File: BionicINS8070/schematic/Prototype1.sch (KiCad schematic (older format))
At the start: 4 parts, among them J1 BionicConnector, U1 INS8070, U2 74HCT126

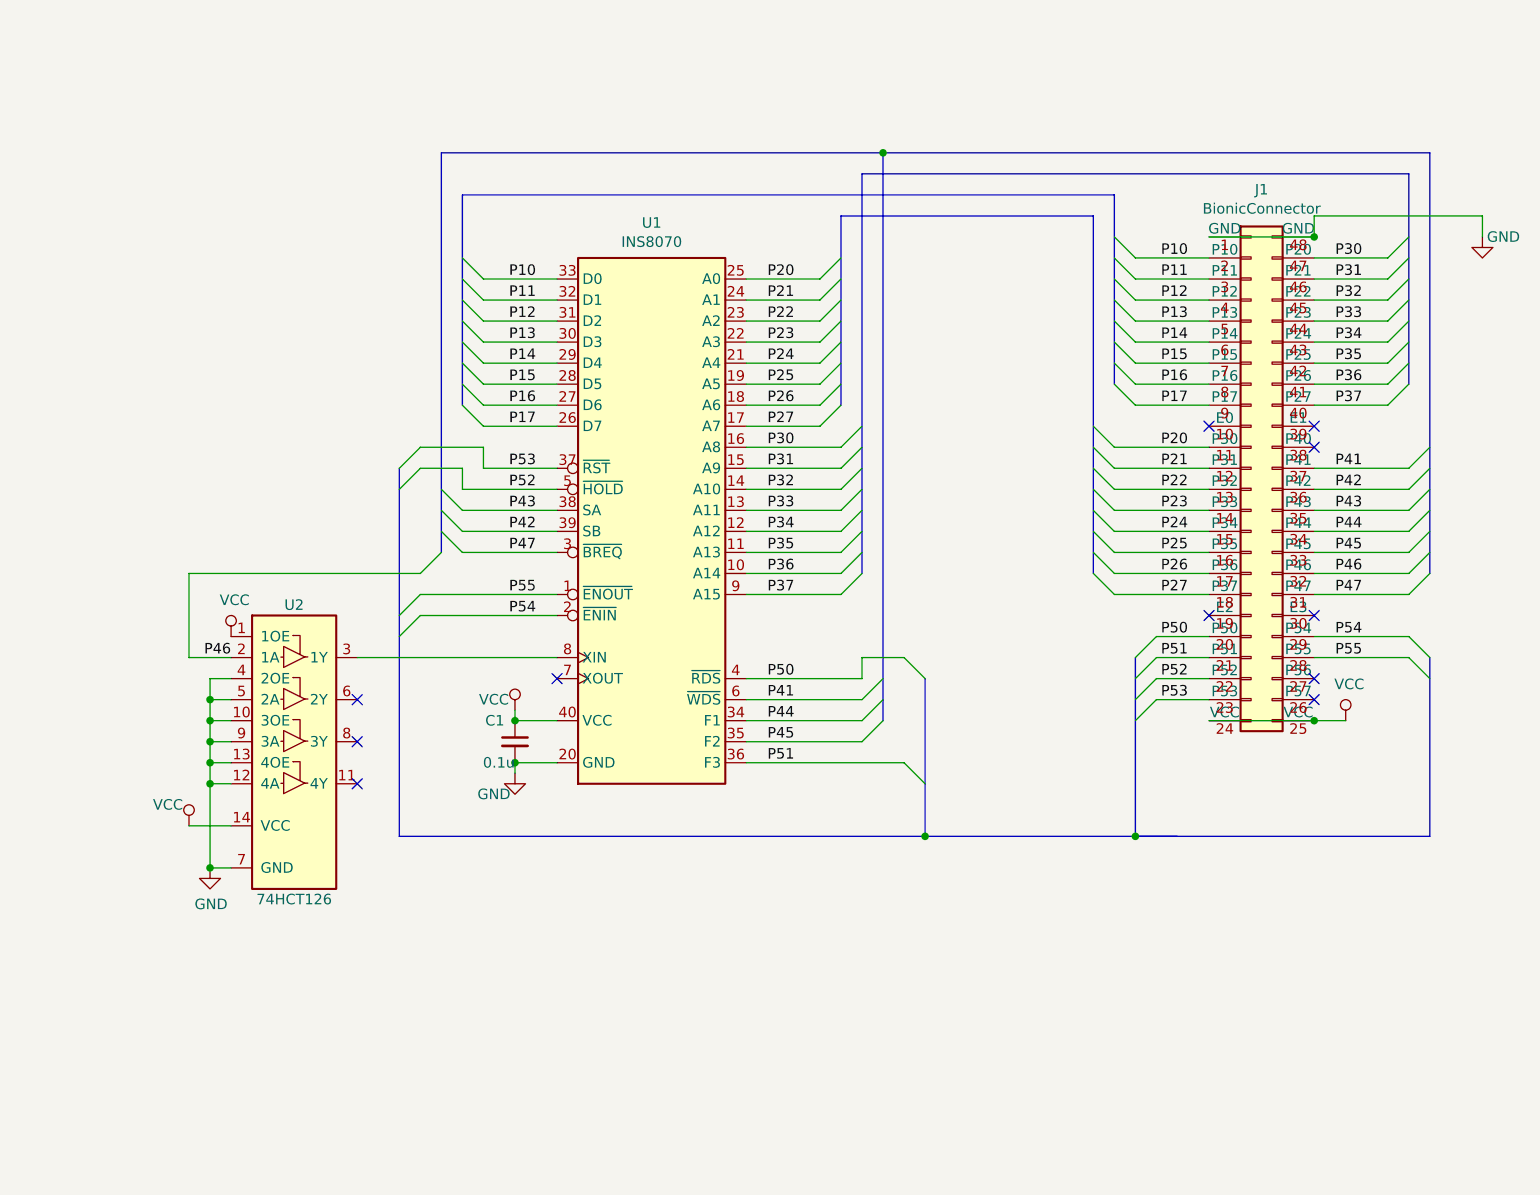
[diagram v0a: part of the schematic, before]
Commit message: Fix Bionic connector pin outs
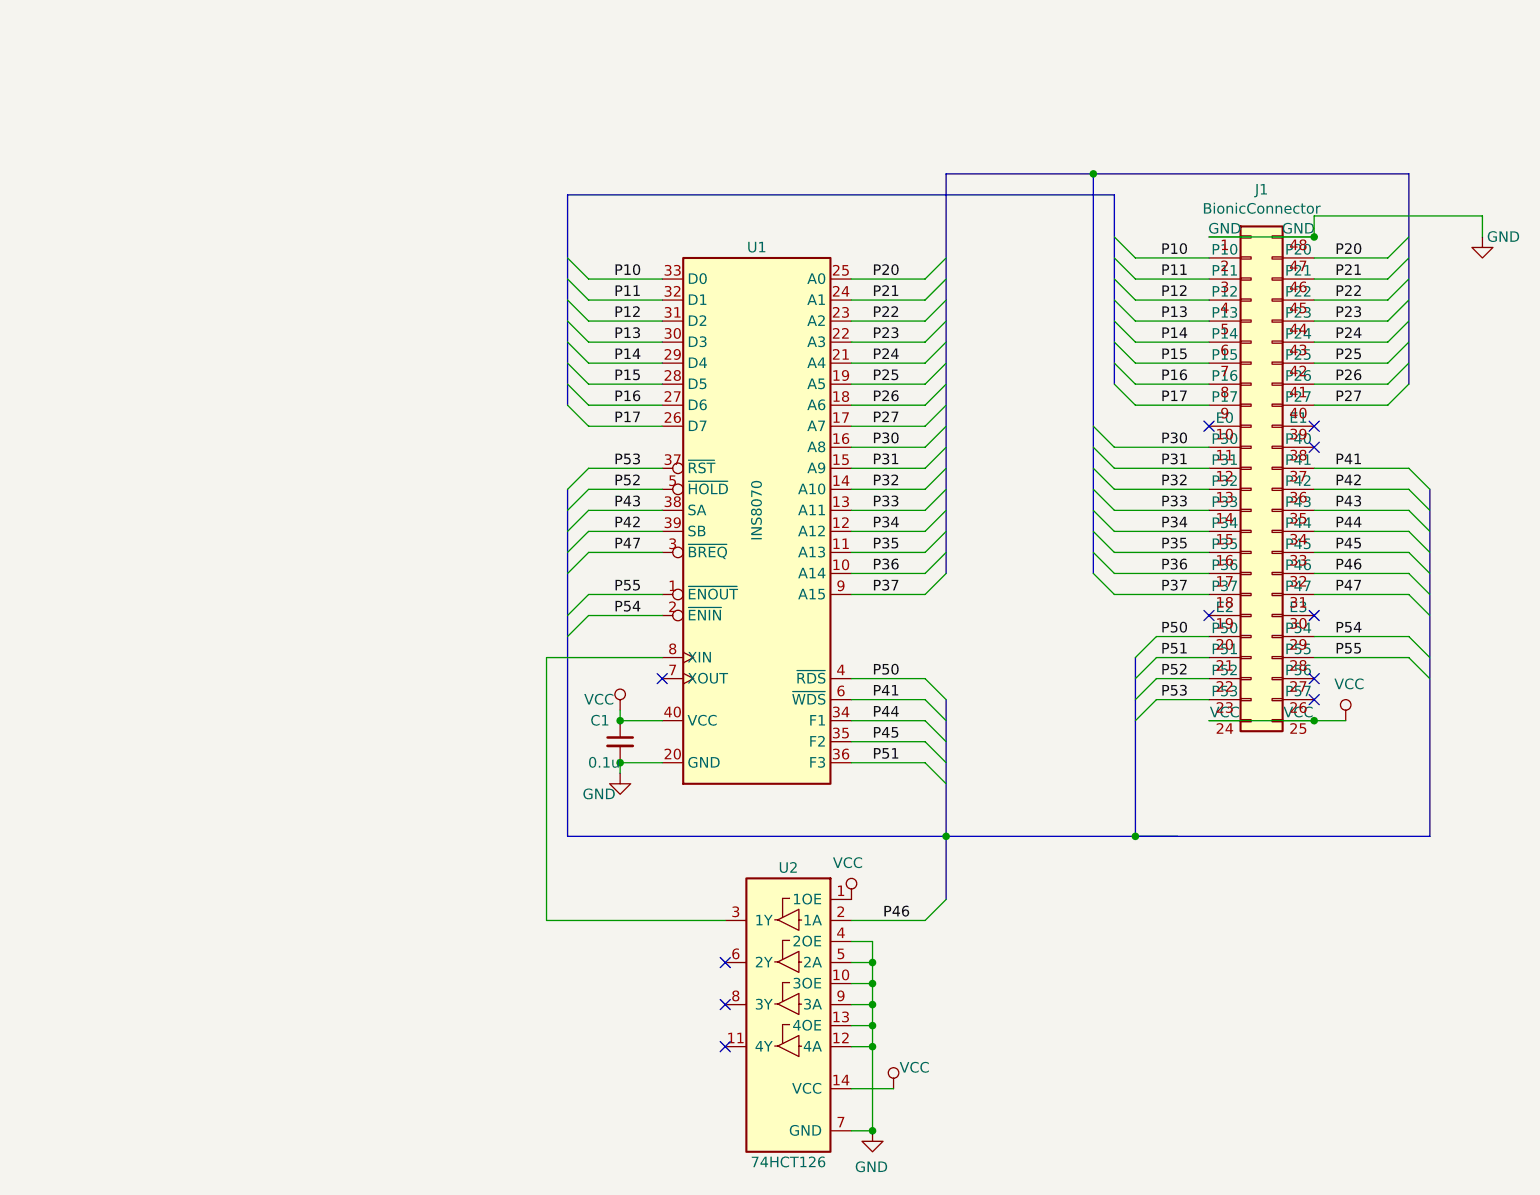
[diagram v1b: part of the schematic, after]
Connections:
- net P20: now also J1.47 (P20); no longer J1.11 (P30)
- net P21: now also J1.46 (P21); no longer J1.12 (P31)
- net P22: now also J1.45 (P22); no longer J1.13 (P32)
- net P23: now also J1.44 (P23); no longer J1.14 (P33)
- net P24: now also J1.43 (P24); no longer J1.15 (P34)
- net P25: now also J1.42 (P25); no longer J1.16 (P35)
- net P26: now also J1.41 (P26); no longer J1.17 (P36)
- net P27: now also J1.40 (P27); no longer J1.18 (P37)
- net P30: now also J1.11 (P30); no longer J1.47 (P20)
- net P31: now also J1.12 (P31); no longer J1.46 (P21)
- net P32: now also J1.13 (P32); no longer J1.45 (P22)
- net P33: now also J1.14 (P33); no longer J1.44 (P23)
- net P34: now also J1.15 (P34); no longer J1.43 (P24)
- net P35: now also J1.16 (P35); no longer J1.42 (P25)
- net P36: now also J1.17 (P36); no longer J1.41 (P26)
- net P37: now also J1.18 (P37); no longer J1.40 (P27)
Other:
- moved on the sheet: C1, U2
